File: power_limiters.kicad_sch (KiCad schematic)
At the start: 31 parts, among them U10 MAX4995AAUT+T, U11 MAX4995AAUT+T, U26 SN74AHC1G02QDCKRQ1, U35 MAX4995AAUT+T, U8 MP5073GG-P, U9 MAX4995AAUT+T

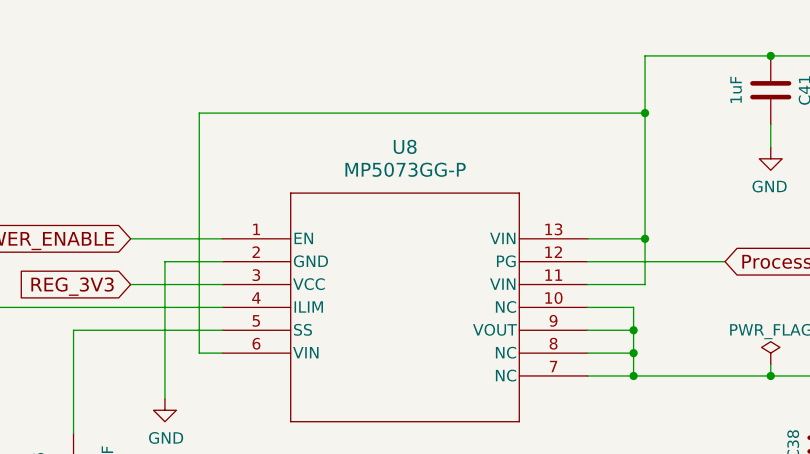
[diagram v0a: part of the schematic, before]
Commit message: Change the 1.2V power limiter to a MPQ5072GG-AEC1
It's 1A max instead of 2A, but should be plenty.  It's automotive
certified.

Signed-off-by: Corey Minyard <corey@minyard.net>
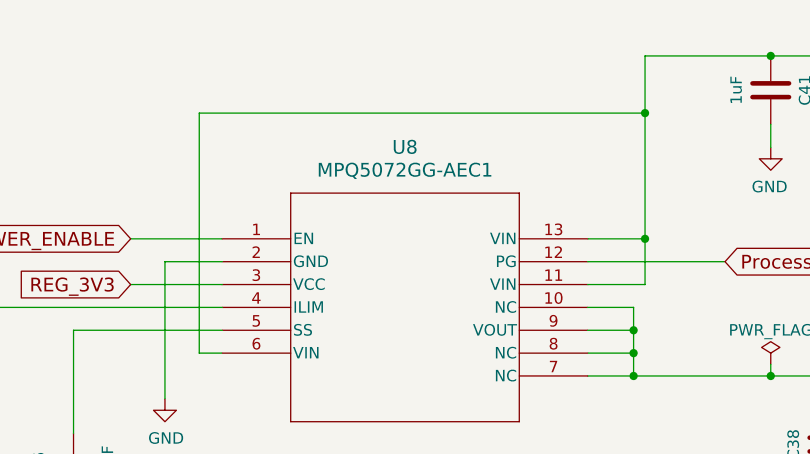
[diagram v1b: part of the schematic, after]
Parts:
- U8: value MP5073GG-P -> MPQ5072GG-AEC1; symbol PACSAT_DEV_misc:MP5073GG-P -> PACSAT_DEV_misc:MPQ5072GG-AEC1
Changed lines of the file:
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@@
 	)
 	(symbol
-		(lib_id "PACSAT_DEV_misc:MP5073GG-P")
+		(lib_id "PACSAT_DEV_misc:MPQ5072GG-AEC1")
 		(at 53.34 49.53 0)
 		(unit 1)
@@
 			)
 		)
-		(property "Value" "MP5073GG-P"
+		(property "Value" "MPQ5072GG-AEC1"
 			(at 73.66 41.91 0)
 			(effects
@@
 			)
 		)
-		(property "Datasheet" "https://www.monolithicpower.com/en/documentview/productdocument/index/version/2/document_type/Datasheet/lang/en/sku/MP5073GG-Z"
+		(property "Datasheet" "https://www.monolithicpower.com/en/documentview/productdocument/index/version/2/document_type/Datasheet/lang/en/sku/MPQ5072GG-AEC1"
 			(at 53.34 49.53 0)
 			(effects

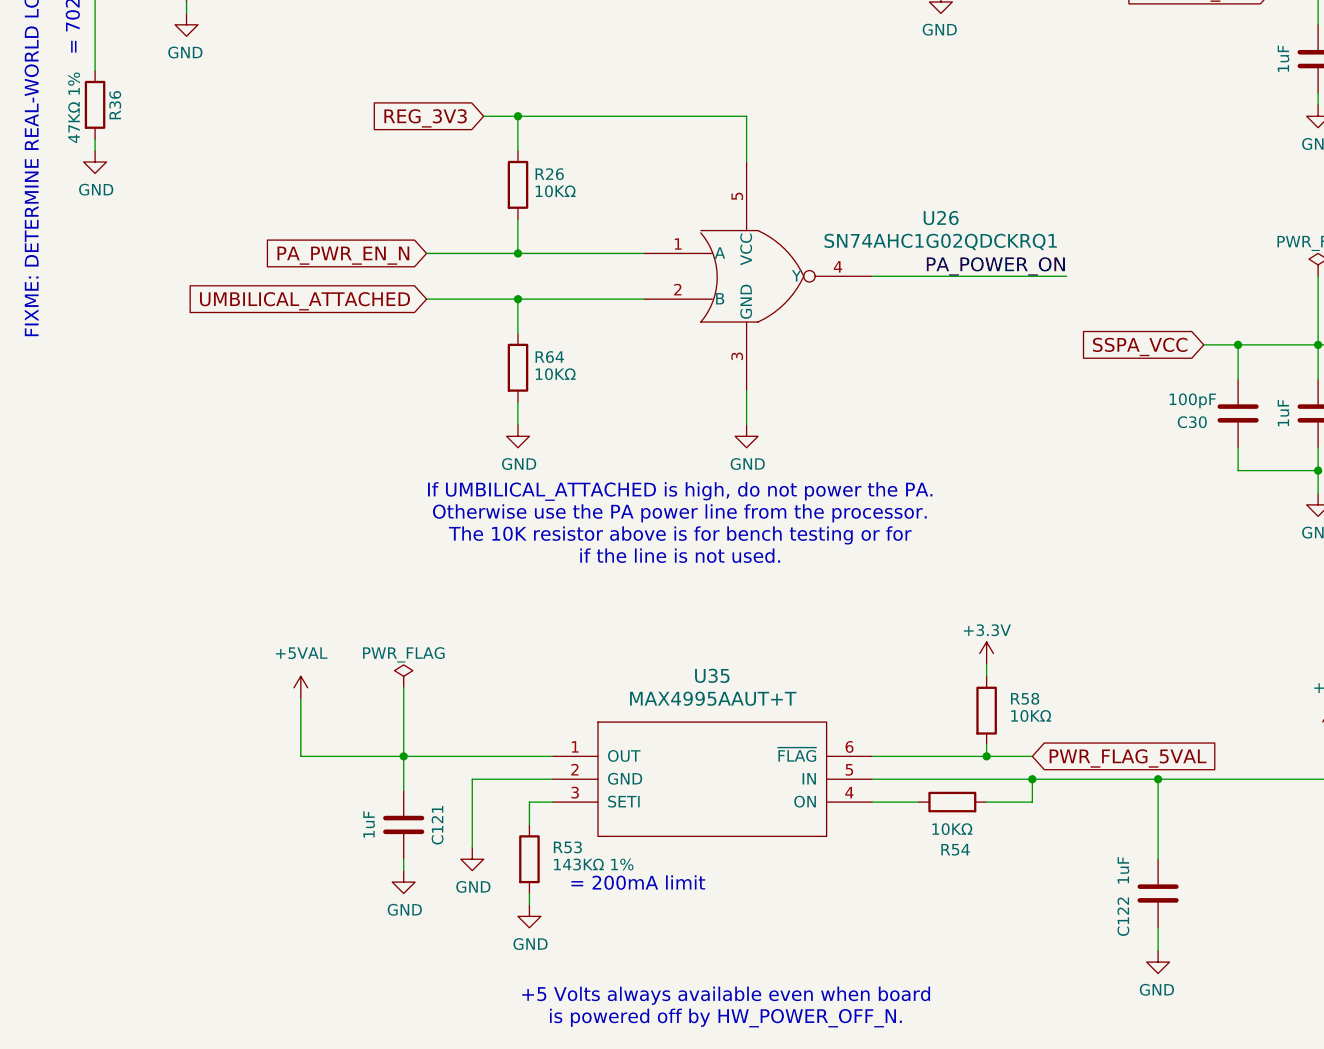
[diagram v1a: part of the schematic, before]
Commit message: Rework the inhibit handling from the ABF lines
Per CubeSat standards from NASA, transmit needs to have three inhibits
The ABF[0-2] lines from the power supplu do this.

Those lines should also power off everything on the board.

So put in logic in to make this happen, and add instructions on how to
lab test.

Signed-off-by: Corey Minyard <corey@minyard.net>
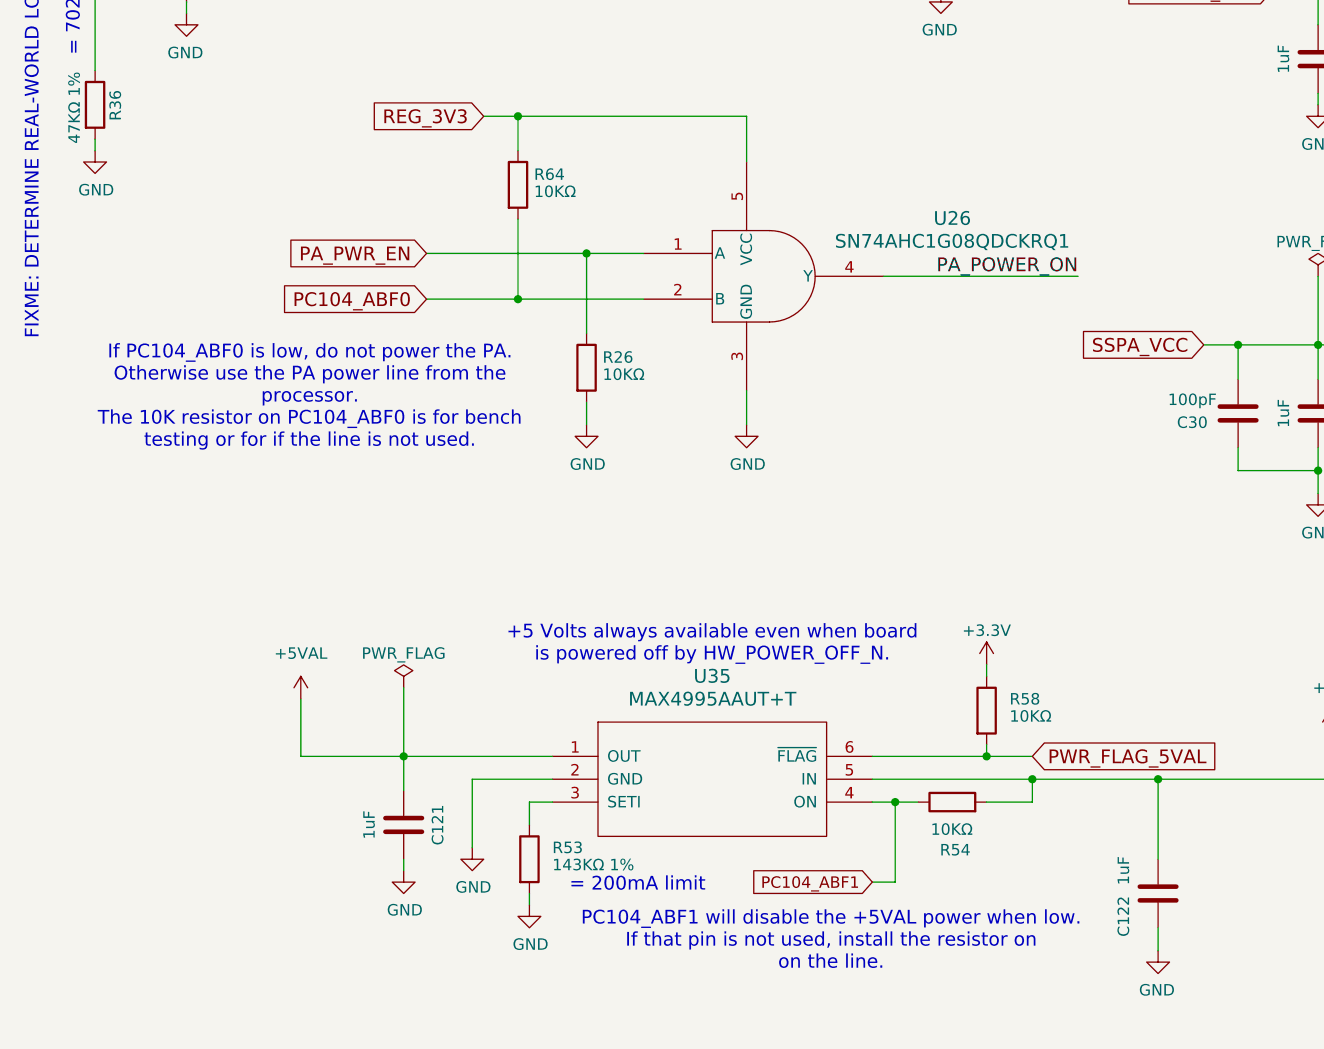
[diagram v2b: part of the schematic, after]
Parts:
- removed U26: SN74AHC1G02QDCKRQ1, PacSatDev_ti:DCK5, symbol PACSAT_ICs:SN74AHC1G02QDCKRQ1
- added U26: SN74AHC1G08QDCKRQ1, PacSatDev_ti:DCK5, symbol PACSAT_ICs:SN74AHC1G08QDCKRQ1
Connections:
- net PA_PWR_EN_N is gone; now on net GND: R26.2
- net UMBILICAL_ATTACHED is gone; now on net REG_3V3: R64.1
- net GND: now also U26.3 (GND); no longer R64.2
- net PA_POWER_ON: now also U26.4 (Y)
- net REG_3V3: now also U26.5 (VCC); no longer R26.1
- net PC104_ABF1: now reaches R54.1, U35.4 (ON)
- new net PA_PWR_EN: R26.1, U26.1 (A)
- new net PC104_ABF0: R64.2, U26.2 (B)
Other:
- note added: "If PC104_ABF0 is low, do not power the PA. Otherwise use the PA power line from the processor. The 10K resistor on PC104_ABF0 is for bench testing or for if the line is not used."
- note added: "PC104_ABF1 will disable the +5VAL power when low. If that pin is not used, install the resistor on on the line."
- note removed: "If UMBILICAL_ATTACHED is high, do not power the PA. Otherwise use the PA power line from the processor. The 10K resistor above is for bench testing or for if the line is not used."
- moved on the sheet: R26, R64

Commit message: Do some renaming
Signed-off-by: Corey Minyard <corey@minyard.net>
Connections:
- net PC104_ABF0 renamed PC104_UMBILICAL0_N
- net PC104_ABF1 renamed PC104_UMBILICAL1_N
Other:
- note added: "If PC104_UMBILICAL0_N is low, do not power the PA. Otherwise use the PA power line from the processor. The 10K resistor on PC104_UMBILICAL0_N is for bench testing or for if the line is not used."
- note added: "PC104_UMBILICAL1_N will disable the +5VAL power when low. If that pin is not used, install the resistor on on the line."
- note removed: "If PC104_ABF0 is low, do not power the PA. Otherwise use the PA power line from the processor. The 10K resistor on PC104_ABF0 is for bench testing or for if the line is not used."
- note removed: "PC104_ABF1 will disable the +5VAL power when low. If that pin is not used, install the resistor on on the line."
- moved on the sheet: C122
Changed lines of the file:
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@@
 		)
 	)
-	(text "If PC104_ABF0 is low, do not power the PA.\nOtherwise use the PA power line from the\nprocessor.\nThe 10K resistor on PC104_ABF0 is for bench\ntesting or for if the line is not used."
+	(text "If PC104_UMBILICAL0_N is low, do not\npower the PA. Otherwise use the PA\npower line from the processor.\nThe 10K resistor on PC104_UMBILICAL0_N is\nfor bench testing or for if the line is\nnot used."
 		(exclude_from_sim no)
 		(at 50.546 122.682 0)
@@
 		)
 	)
-	(text "PC104_ABF1 will disable the +5VAL power when low.\nIf that pin is not used, install the resistor on\non the line."
+	(text "PC104_UMBILICAL1_N will disable the +5VAL\npower when low. If that pin is not used,\ninstall the resistor on on the line."
 		(exclude_from_sim no)
 		(at 108.458 183.134 0)
@@
 	)
 	(junction
-		(at 162.56 130.81)
+		(at 152.4 165.1)
 		(diameter 0)
 		(color 0 0 0 0)
 	)
 	(junction
-		(at 144.78 165.1)
+		(at 162.56 130.81)
 		(diameter 0)
 		(color 0 0 0 0)
@@
 	(wire
 		(pts
-			(xy 144.78 165.1) (xy 163.83 165.1)
-		)
-		(stroke
-			(width 0)
-			(type default)
-		)
-	)
-	(wire
-		(pts
 			(xy 257.81 38.1) (xy 257.81 40.64)
 		)
@@
 	(wire
 		(pts
-			(xy 144.78 184.15) (xy 144.78 181.61)
+			(xy 152.4 184.15) (xy 152.4 181.61)
 		)
 		(stroke
@@
 	(wire
 		(pts
-			(xy 144.78 173.99) (xy 144.78 165.1)
+			(xy 152.4 173.99) (xy 152.4 165.1)
 		)
 		(stroke
@@
 	(wire
 		(pts
-			(xy 130.81 165.1) (xy 144.78 165.1)
+			(xy 130.81 165.1) (xy 152.4 165.1)
 		)
 		(stroke
@@
 	(wire
 		(pts
-			(xy 113.03 176.53) (xy 115.57 176.53)
+			(xy 118.11 176.53) (xy 115.57 176.53)
 		)
 		(stroke
@@
 	(wire
 		(pts
+			(xy 152.4 165.1) (xy 163.83 165.1)
+		)
+		(stroke
+			(width 0)
+			(type default)
+		)
+	)
+	(wire
+		(pts
 			(xy 53.34 52.07) (xy 46.99 52.07)
 		)
@@
 		)
 	)
-	(global_label "PC104_ABF0"
+	(global_label "PC104_UMBILICAL0_N"
 		(shape input)
 		(at 63.5 111.76 180)
@@
 		)
 		(property "Intersheetrefs" "${INTERSHEET_REFS}"
-			(at 46.5519 111.76 0)
+			(at 36.3194 111.76 0)
 			(effects
 				(font
@@
 		)
 	)
-	(global_label "PC104_ABF1"
+	(global_label "PC104_UMBILICAL1_N"
 		(shape input)
-		(at 113.03 176.53 180)
+		(at 118.11 176.53 0)
 		(fields_autoplaced yes)
 		(effects
@@
 				(size 1.27 1.27)
 			)
-			(justify right)
+			(justify left)
 		)
 		(property "Intersheetrefs" "${INTERSHEET_REFS}"
-			(at 98.9062 176.53 0)
+			(at 140.761 176.53 0)
 			(effects
 				(font
 					(size 1.27 1.27)
 				)
-				(justify right)
+				(justify left)
 				(hide yes)
 			)
@@
 	(symbol
 		(lib_id "power:GND")
-		(at 144.78 184.15 0)
+		(at 152.4 184.15 0)
 		(mirror y)
 		(unit 1)
@@
 		(dnp no)
 		(property "Reference" "#PWR0278"
-			(at 144.78 190.5 0)
+			(at 152.4 190.5 0)
 			(effects
 				(font
@@
 		)
 		(property "Value" "GND"
-			(at 144.653 188.5442 0)
+			(at 152.273 188.5442 0)
 			(effects
 				(font
@@
 		)
 		(property "Footprint" ""
-			(at 144.78 184.15 0)
+			(at 152.4 184.15 0)
 			(effects
 				(font
@@
 		)
 		(property "Datasheet" ""
-			(at 144.78 184.15 0)
+			(at 152.4 184.15 0)
 			(effects
 				(font
@@
 		)
 		(property "Description" ""
-			(at 144.78 184.15 0)
+			(at 152.4 184.15 0)
 			(effects
 				(font
@@
 	(symbol
 		(lib_id "Device:C")
-		(at 144.78 177.8 0)
+		(at 152.4 177.8 0)
 		(mirror y)
 		(unit 1)
@@
 		(dnp no)
 		(property "Reference" "C122"
-			(at 140.97 180.34 90)
+			(at 148.59 180.34 90)
 			(effects
 				(font
@@
 		)
 		(property "Value" "1uF"
-			(at 140.97 175.26 90)
+			(at 148.59 175.26 90)
 			(effects
 				(font
@@
 		)
 		(property "Footprint" "Capacitor_SMD:C_0805_2012Metric_Pad1.18x1.45mm_HandSolder"
-			(at 143.8148 181.61 0)
+			(at 151.4348 181.61 0)
 			(effects
 				(font
@@
 		)
 		(property "Datasheet" "~"
-			(at 144.78 177.8 0)
+			(at 152.4 177.8 0)
 			(effects
 				(font
@@
 		)
 		(property "Description" ""
-			(at 144.78 177.8 0)
+			(at 152.4 177.8 0)
 			(effects
 				(font

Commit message: Get the board ready for operation
Make the board ready as a final product, remove the lab testing portions
and add in the things required for full operation.

Signed-off-by: Corey Minyard <corey@minyard.net>
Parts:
- R54, R64: now not fitted; now left out of the parts list
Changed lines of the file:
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@@
 		(unit 1)
 		(exclude_from_sim no)
-		(in_bom yes)
-		(on_board yes)
-		(dnp no)
+		(in_bom no)
+		(on_board yes)
+		(dnp yes)
 		(property "Reference" "R54"
 			(at 123.952 172.974 90)
@@
 		(unit 1)
 		(exclude_from_sim no)
-		(in_bom yes)
-		(on_board yes)
-		(dnp no)
+		(in_bom no)
+		(on_board yes)
+		(dnp yes)
 		(property "Reference" "R64"
 			(at 75.438 97.917 0)

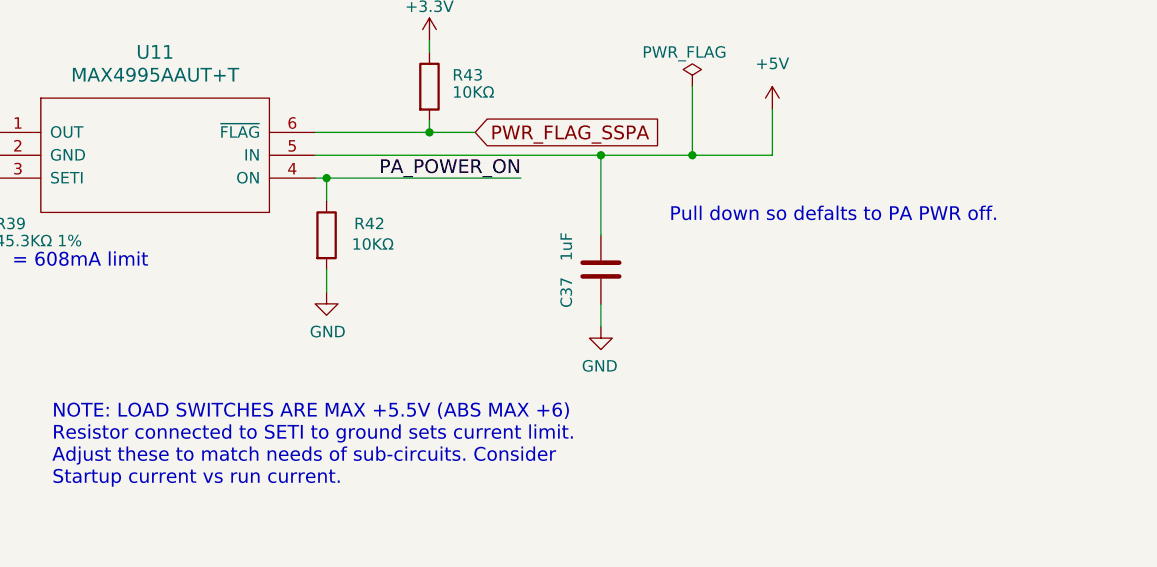
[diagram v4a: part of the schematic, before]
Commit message: Fix the symbol name on the SPI/I2C converter
Signed-off-by: Corey Minyard <corey@minyard.net>
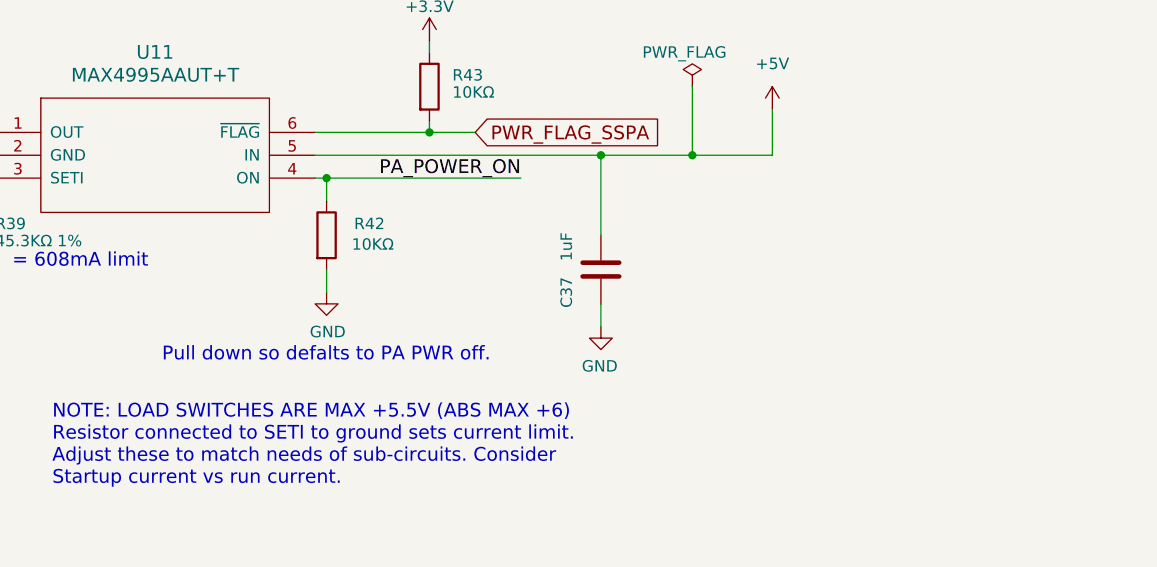
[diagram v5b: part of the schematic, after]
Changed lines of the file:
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@@
 	(text "Pull down so defalts to PA PWR off."
 		(exclude_from_sim no)
-		(at 254 127 0)
+		(at 197.612 142.494 0)
 		(effects
 			(font

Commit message: Parts replacements for out of stock parts
Signed-off-by: Corey Minyard <corey@minyard.net>
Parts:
- U8: value MPQ5072GG-AEC1 -> MPQ5072GG-AEC1-Z
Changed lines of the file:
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@@
 			)
 		)
-		(property "Value" "MPQ5072GG-AEC1"
+		(property "Value" "MPQ5072GG-AEC1-Z"
 			(at 73.66 41.91 0)
 			(effects
